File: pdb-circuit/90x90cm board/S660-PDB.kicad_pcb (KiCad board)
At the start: 2 copper layers, 90 x 90 mm, 45 parts, among them J1 PWR INPUT, J2 PWR OUTPUT, J3 JST-XH 6p to Pi, K1 G2RL-1A DC12, Q2 BC337-40, Q3 2N7000, U1 ATtiny85-20P, U2 LM2936Z-3.3, U3 PC817

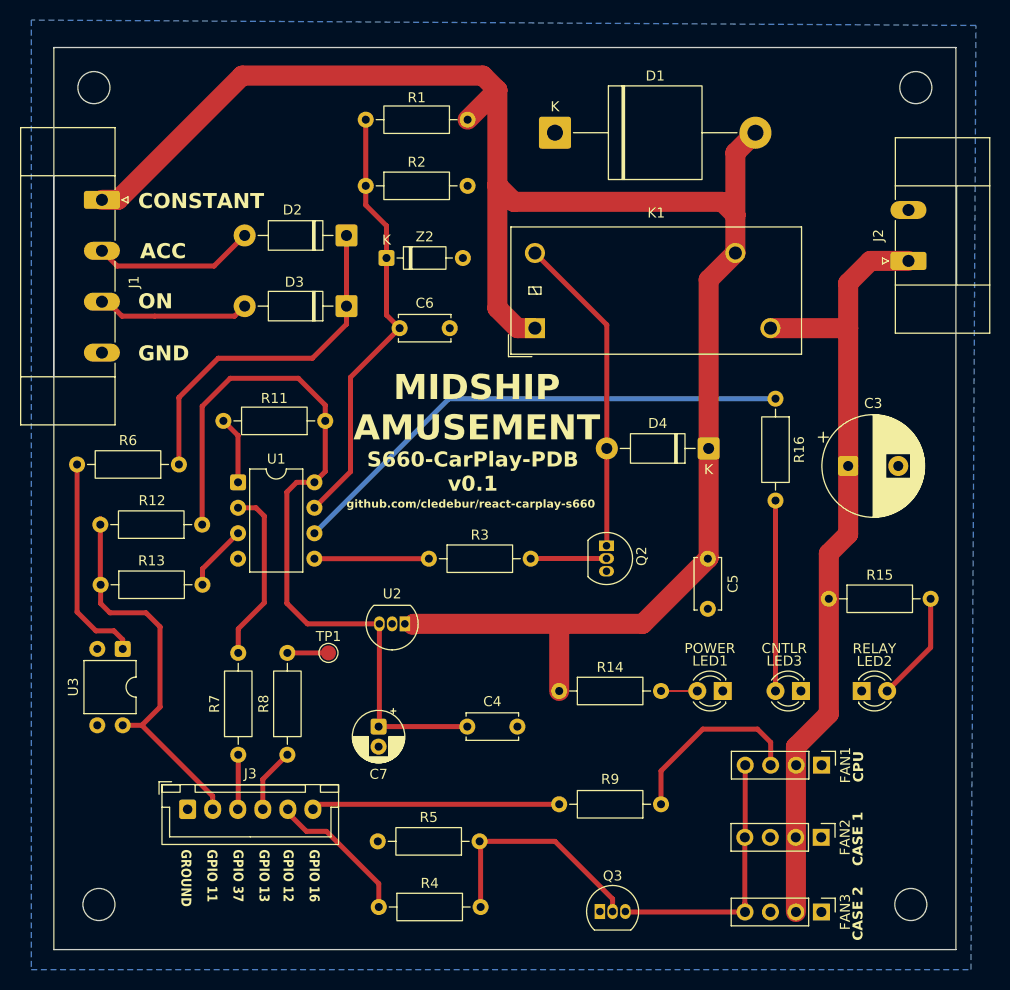
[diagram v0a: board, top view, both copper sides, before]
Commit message: PDB rev D: schematic/PCB updates, review notes, BOM/CPL, gerbers and assembly package
Co-Authored-By: Claude Opus 5.5 <noreply@anthropic.com>
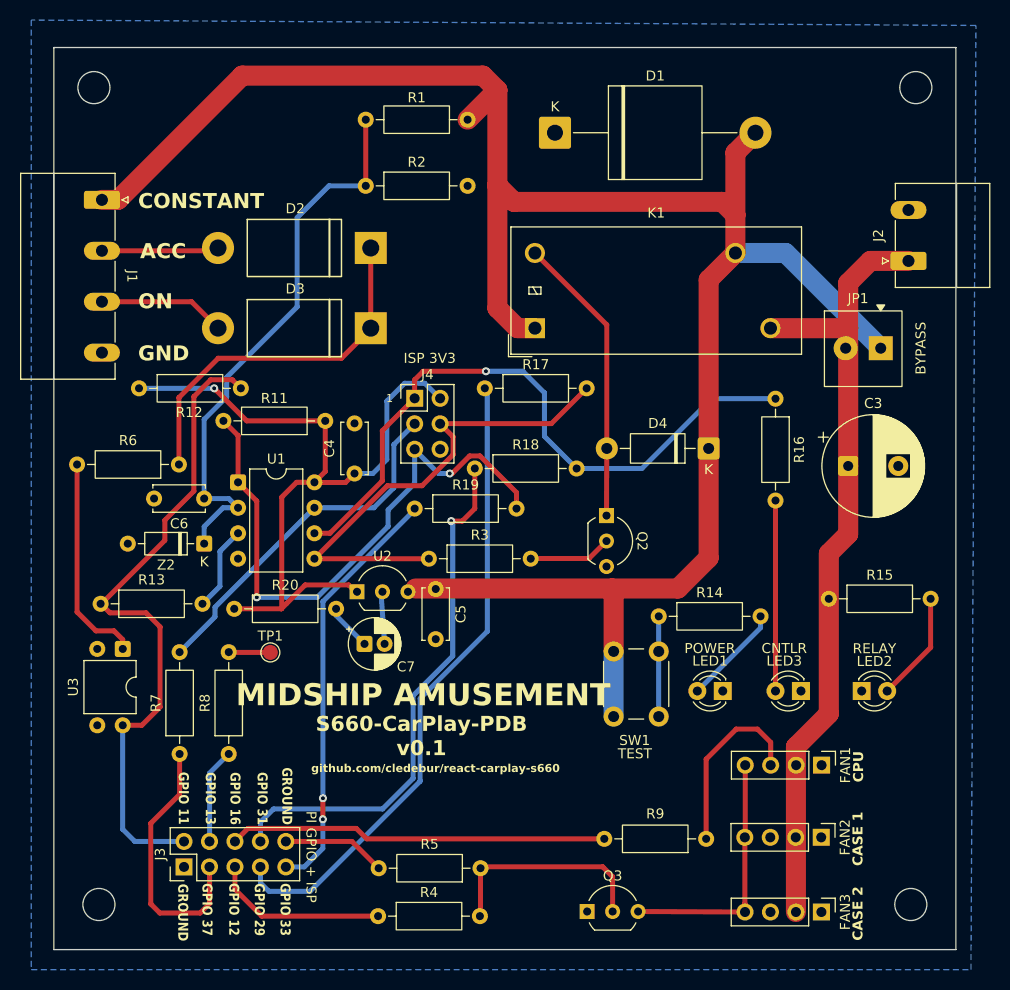
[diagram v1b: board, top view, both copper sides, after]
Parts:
- added J4: AVR ISP 3V3, Connector_PinHeader_2.54mm:PinHeader_2x03_P2.54mm_Vertical, F.Cu at (48.0, 47.0)
- added JP1: RELAY BYPASS, S660-PDB:Phoenix_MKDS_1_2_3.5_1751248, F.Cu at (94.5, 42.0)
- added R17: 1k, Resistor_THT:R_Axial_DIN0207_L6.3mm_D2.5mm_P10.16mm_Horizontal, F.Cu at (55.0, 46.0)
- added R18: 1k, Resistor_THT:R_Axial_DIN0207_L6.3mm_D2.5mm_P10.16mm_Horizontal, F.Cu at (54.0, 54.0)
- added R19: 1k, Resistor_THT:R_Axial_DIN0207_L6.3mm_D2.5mm_P10.16mm_Horizontal, F.Cu at (48.0, 58.0)
- added R20: 1R, Resistor_THT:R_Axial_DIN0207_L6.3mm_D2.5mm_P10.16mm_Horizontal, F.Cu at (30.0, 68.0)
- added SW1: PUSH TO TEST, Button_Switch_THT:SW_PUSH_6mm_H4.3mm, F.Cu at (72.3, 72.2)
- C7: value 10uF 25V -> 47uF 25V
- D2, D3: value SS34 -> 1N5822; footprint Diode_THT:D_DO-41_SOD81_P10.16mm_Horizontal -> S660-PDB:D_Multicomp_1N5822_DO27_P15.24mm
- J1: footprint Connector_Phoenix_MC_HighVoltage:PhoenixContact_MC_1,5_4-GF-5.08_1x04_P5.08mm_Horizontal_ThreadedFlange -> Connector_Phoenix_MC_HighVoltage:PhoenixContact_MC_1,5_4-G-5.08_1x04_P5.08mm_Horizontal
- J2: footprint Connector_Phoenix_MC_HighVoltage:PhoenixContact_MC_1,5_2-GF-5.08_1x02_P5.08mm_Horizontal_ThreadedFlange -> Connector_Phoenix_MC_HighVoltage:PhoenixContact_MC_1,5_2-G-5.08_1x02_P5.08mm_Horizontal
- J3: value JST-XH 6p to Pi -> Pi interface / ISP; footprint Connector_JST:JST_XH_B6B-XH-A_1x06_P2.50mm_Vertical -> Connector_PinHeader_2.54mm:PinHeader_2x05_P2.54mm_Vertical
- Q2, Q3, U2: footprint Package_TO_SOT_THT:TO-92_Inline -> Package_TO_SOT_THT:TO-92_Inline_Wide
- moved Z2 33.8 mm to (27.0, 61.5), turned to 180 degrees
- moved C4 27.6 mm to (42.0, 54.5), turned to 90 degrees
- moved C5 27.3 mm to (50.1, 66.0)
- moved C6 25.9 mm to (27.0, 57.0), turned to 180 degrees
- moved R12 15.0 mm to (20.5, 46.0), turned to 0 degrees
- moved R14 12.4 mm to (72.3, 68.8)
- moved C7 8.37 mm to (43.0, 71.5), turned to 0 degrees
- moved R7 5.85 mm to (24.6, 82.5)
- moved R8 5.85 mm to (29.4, 82.5)
- moved TP1 5.80 mm to (33.6, 72.3)
- moved J3 5.76 mm to (25.0, 93.8), turned to 90 degrees
- moved U2 5.74 mm to (42.2, 66.3), turned to 0 degrees
- moved R9 5.67 mm to (77.1, 91.0)
- moved D3 5.65 mm to (36.0, 40.0)
- moved D2 5.35 mm to (36.0, 32.0)
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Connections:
- C7 pad 1: /3V3 -> Net-(C7-Pad1)
- R14 pad 1: /12V_IN -> /LED_TEST
- U1 pad 2: /HALT_IN -> /BATT_SENSE
- U1 pad 7: /BATT_SENSE -> /HALT_IN
- U2 pad 1: /12V_IN -> /3V3
- U2 pad 3: /3V3 -> /12V_IN
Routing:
- net /J3_MOSI: track 0.00 -> 64.2 mm
- net /J3_MISO: track 0.00 -> 53.2 mm, vias 0 -> 1
- net /nRESET: track 6.73 -> 58.8 mm, vias 0 -> 2
- net /J3_RESET: track 0.00 -> 42.0 mm, vias 0 -> 2
- net /COIL_DRV: track 11.4 -> 49.2 mm
- net /IGN_STATE: track 39.5 -> 66.6 mm
- net /12V_IN: track 184.0 -> 207.8 mm
- net /J3_HALT: track 5.39 -> 26.4 mm
- net /HALT_IN: track 17.7 -> 36.0 mm
- net GND: track 0.00 -> 15.6 mm
- net /LED3_DRV: track 51.6 -> 66.2 mm, vias 0 -> 1
- net /TACH: track 24.1 -> 37.8 mm
- net /BATT_SENSE: track 43.6 -> 56.2 mm
- net /LED_TEST: track 0.00 -> 10.0 mm
- net Net-(LED1-A): track 3.62 -> 10.1 mm
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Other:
- board text added: "1"
- board text added: "BYPASS"
- board text added: "GPIO 29"
- board text added: "GPIO 31"
- board text added: "GPIO 33"
- board text added: "ISP 3V3"
- board text added: "PI GPIO + ISP"
- board text added: "TEST"
